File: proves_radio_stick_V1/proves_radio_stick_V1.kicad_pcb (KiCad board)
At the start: 4 copper layers, 60.7 x 30.9 mm, 61 parts, among them J1 SWD Port, J12 USB_C_Receptacle_USB2.0_16P, J2 Conn_Coaxial, J22 SWD Port, SW1 KMR2, SW2 KMR2, U11 W25Q128JVS, U18 RP2350_60QFN, U2 TPS62085RLTT, U3 E32-400M20S_C2965514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

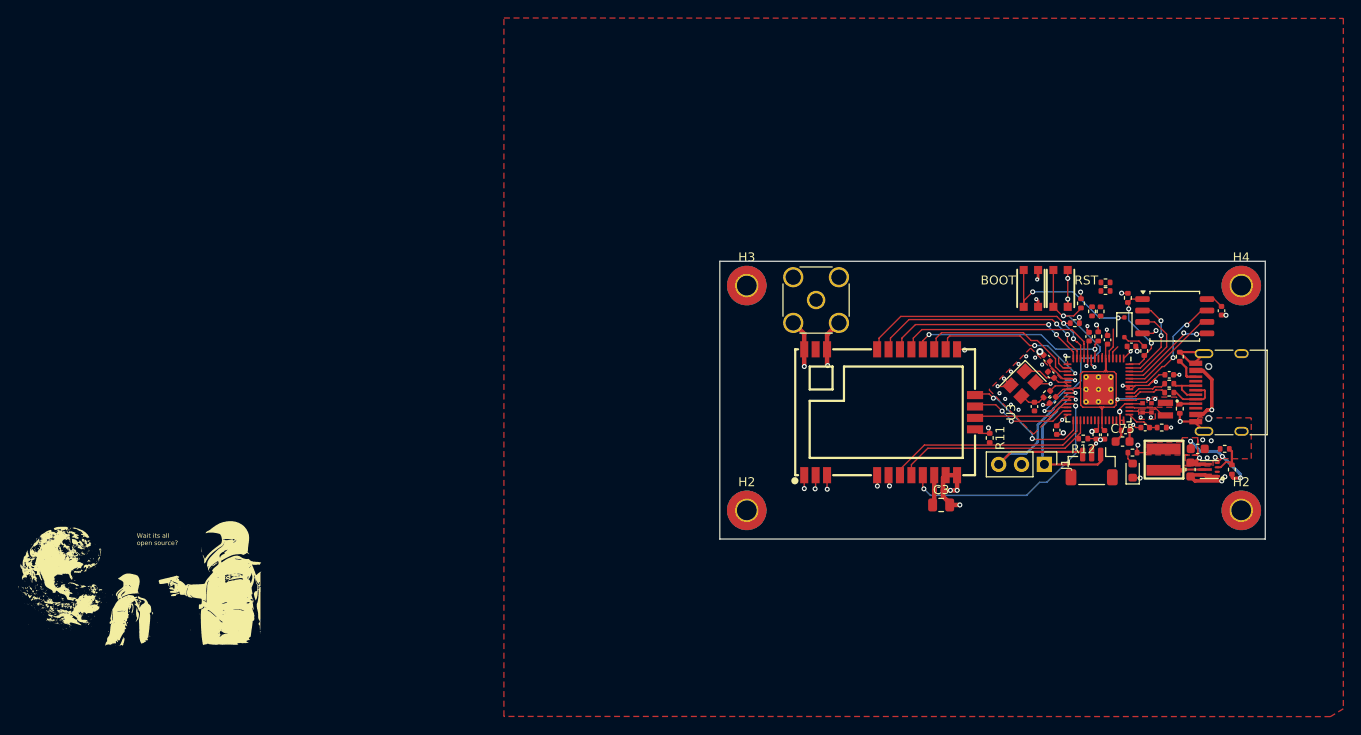
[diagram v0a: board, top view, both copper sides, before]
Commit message: Updated with Screw Terminals and Vias
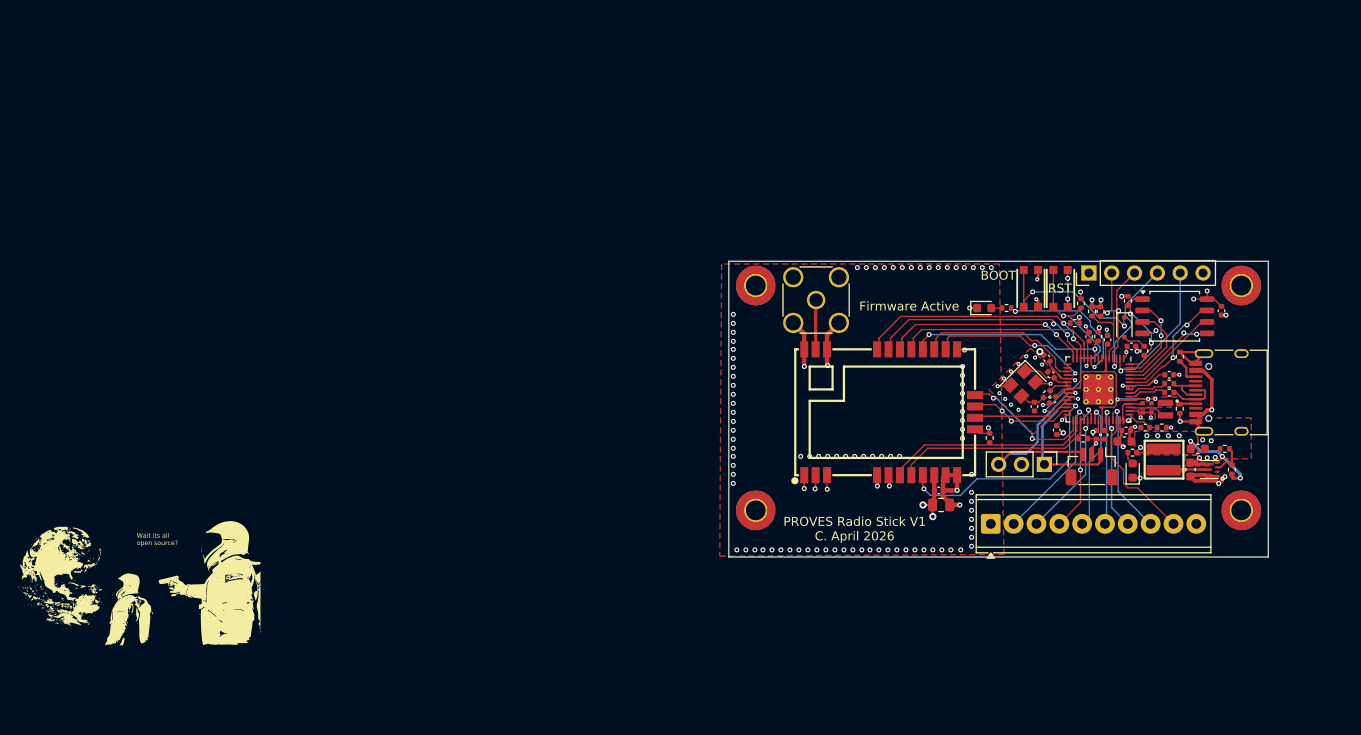
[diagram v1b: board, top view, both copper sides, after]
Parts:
- removed the H2 at (167.0, 112.0)
- removed R25, R6: 10k, Resistor_SMD:R_0402_1005Metric
- added D1: LED, LED_SMD:LED_0603_1608Metric, F.Cu at (193.4, 89.5)
- added H1: MountingHole, MountingHole:MountingHole_2.2mm_M2_Pad_TopBottom, F.Cu at (168.0, 112.0)
- added J3: Screw_Terminal_01x10, TerminalBlock_Phoenix:TerminalBlock_Phoenix_MPT-0,5-10-2.54_1x10_P2.54mm_Horizontal, F.Cu at (194.1, 113.5)
- added J4: Conn_01x06_Pin, Connector_PinHeader_2.54mm:PinHeader_1x06_P2.54mm_Vertical, F.Cu at (205.1, 85.6)
- added R13: 1k, Resistor_SMD:R_0402_1005Metric, F.Cu at (195.9, 89.5)
- R80: value 10k -> 1k
- moved H3 1.00 mm to (168.0, 87.0)
- moved R2 0.33 mm to (209.4, 88.7)
- moved C75 0.20 mm to (209.0, 104.3)
- moved C76 0.07 mm to (209.2, 103.1)
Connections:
- U18 pad 10: unconnected-(U18-GPIO7-Pad10) -> Firmware_Active
- U18 pad 34: unconnected-(U18-GPIO22-Pad34) -> GPIO22
- U18 pad 35: unconnected-(U18-GPIO23-Pad35) -> GPIO23
- U18 pad 36: unconnected-(U18-GPIO24-Pad36) -> GPIO24
- U18 pad 37: unconnected-(U18-GPIO25-Pad37) -> GPIO25
- U18 pad 40: unconnected-(U18-GPIO26_ADC0-Pad40) -> GPIO26
- U18 pad 41: unconnected-(U18-GPIO27_ADC1-Pad41) -> GPIO27
- U18 pad 42: unconnected-(U18-GPIO28_ADC2-Pad42) -> GPIO28
- U18 pad 43: unconnected-(U18-GPIO29_ADC3-Pad43) -> GPIO29
- U18 pad 7: SDA0 -> unconnected-(U18-GPIO4-Pad7)
- U18 pad 8: SCL0 -> unconnected-(U18-GPIO5-Pad8)
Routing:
- net Firmware_Active: track 0.00 -> 16.7 mm, vias 0 -> 2
- net GPIO22: track 0.00 -> 16.7 mm, vias 0 -> 1
- net TX: track 0.00 -> 15.9 mm, vias 0 -> 1
- net GPIO28: track 0.00 -> 15.4 mm, vias 0 -> 1
- net GPIO29: track 0.00 -> 15.3 mm
- net GPIO24: track 0.00 -> 15.3 mm, vias 0 -> 2
- net GPIO25: track 0.00 -> 14.4 mm, vias 0 -> 1
- net RX: track 0.00 -> 13.9 mm, vias 0 -> 1
- net GPIO23: track 0.00 -> 13.9 mm, vias 0 -> 1
- net GPIO26: track 0.00 -> 13.4 mm, vias 0 -> 1
- net GPIO27: track 0.00 -> 12.4 mm, vias 0 -> 1
- net SDA1: track 1.53 -> 12.9 mm, vias 0 -> 2
- net SCL1: track 3.46 -> 12.6 mm
- net +3V3: track 57.2 -> 63.3 mm, vias 17 -> 28
- net Net-(J2-In): track 0.00 -> 5.50 mm
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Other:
- board size 60.7 x 30.9 mm -> 60 x 32.9 mm
- board text added: "1 2 3 4 5 6 7 . . . How many more days until the weekend? 1 2 3 Now I'm in the studio looking at your image . . ."
- board text added: "22"
- board text added: "23"
- board text added: "24"
- board text added: "25"
- board text added: "26"
- board text added: "27"
- board text added: "28"
- board text added: "29"
- board text added: "A"
- board text added: "D"
- board text added: "Firmware Active"
- board text added: "GND"
- board text added: "PROVES Radio Stick V1 C. April 2026"

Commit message: Updated Prod Files
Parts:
- added TP1: TestPoint, TestPoint:TestPoint_Keystone_5000-5004_Miniature, F.Cu at (187.5, 87.0)
- added TP2: TestPoint, TestPoint:TestPoint_Keystone_5000-5004_Miniature, F.Cu at (180.6, 90.8)
- added TP3: TestPoint, TestPoint:TestPoint_Keystone_5000-5004_Miniature, F.Cu at (180.6, 87.0)
- added TP4: TestPoint, TestPoint:TestPoint_Keystone_5000-5004_Miniature, F.Cu at (184.0, 87.0)
- added TP5: TestPoint, TestPoint:TestPoint_Keystone_5000-5004_Miniature, F.Cu at (191.0, 87.0)
- added TP6: TestPoint, TestPoint:TestPoint_Keystone_5000-5004_Miniature, F.Cu at (194.5, 87.0)
- added TP7: TestPoint, TestPoint:TestPoint_Keystone_5000-5004_Miniature, F.Cu at (195.1, 94.7)
- moved R11 3.78 mm to (197.8, 104.0)
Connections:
- J22 pad 1: SWDIO -> SWCLK
- J22 pad 3: SWCLK -> SWDIO
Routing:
- net RF1_IO1: track 18.1 -> 26.5 mm
- net RF1_IO0: track 18.2 -> 24.6 mm, vias 0 -> 1
- net SPI1_MISO: track 22.9 -> 29.2 mm, vias 0 -> 1
- net SPI1_SCK: track 25.6 -> 31.8 mm, vias 2 -> 3
- net RF1_RST: track 23.2 -> 29.2 mm, vias 2 -> 3
- net SPI1_MOSI: track 22.8 -> 28.3 mm, vias 2 -> 3
- net SWCLK: track 24.0 -> 27.1 mm
- net SWDIO: track 18.2 -> 15.8 mm
- net SPI1_CS0: track 28.4 -> 30.7 mm
- net GND: track 86.0 -> 88.2 mm, vias 139 -> 140
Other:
- board text added: "1 2 3 4 5 6 7 . . . How many more days until the weekend? 1 2 3 What's the fee for the damage? Now I'm in the studio looking at your image . . ."
- board text added: "CS0"
- board text added: "DIO0"
- board text added: "DIO1"
- board text added: "Ebyte E32-400M20S"
- board text added: "MISO"
- board text added: "MOSI"
- board text added: "RF_RST"
- board text added: "SCK"
- board text removed: "1 2 3 4 5 6 7 . . . How many more days until the weekend? 1 2 3 Now I'm in the studio looking at your image . . ."
- board text removed: "BOOT"
- board text removed: "Firmware Active"
